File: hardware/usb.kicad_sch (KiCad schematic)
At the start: 4 parts

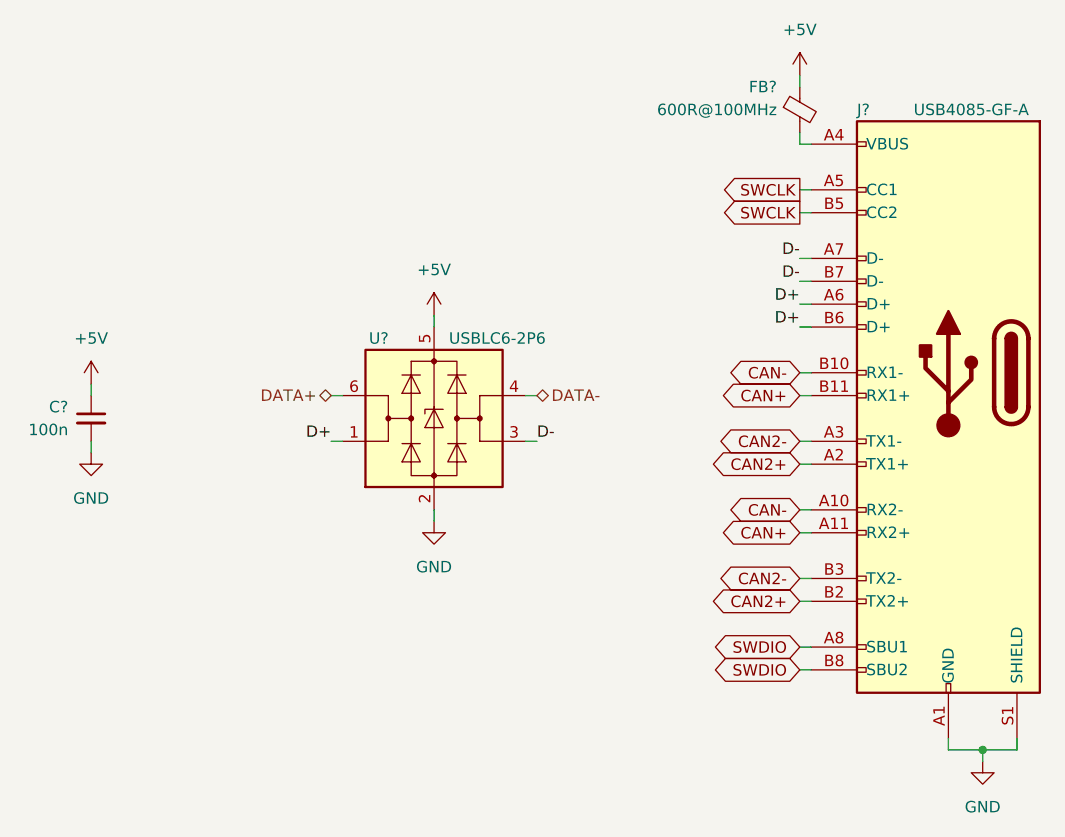
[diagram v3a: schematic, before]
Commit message: Improve the schematic according to the feedback
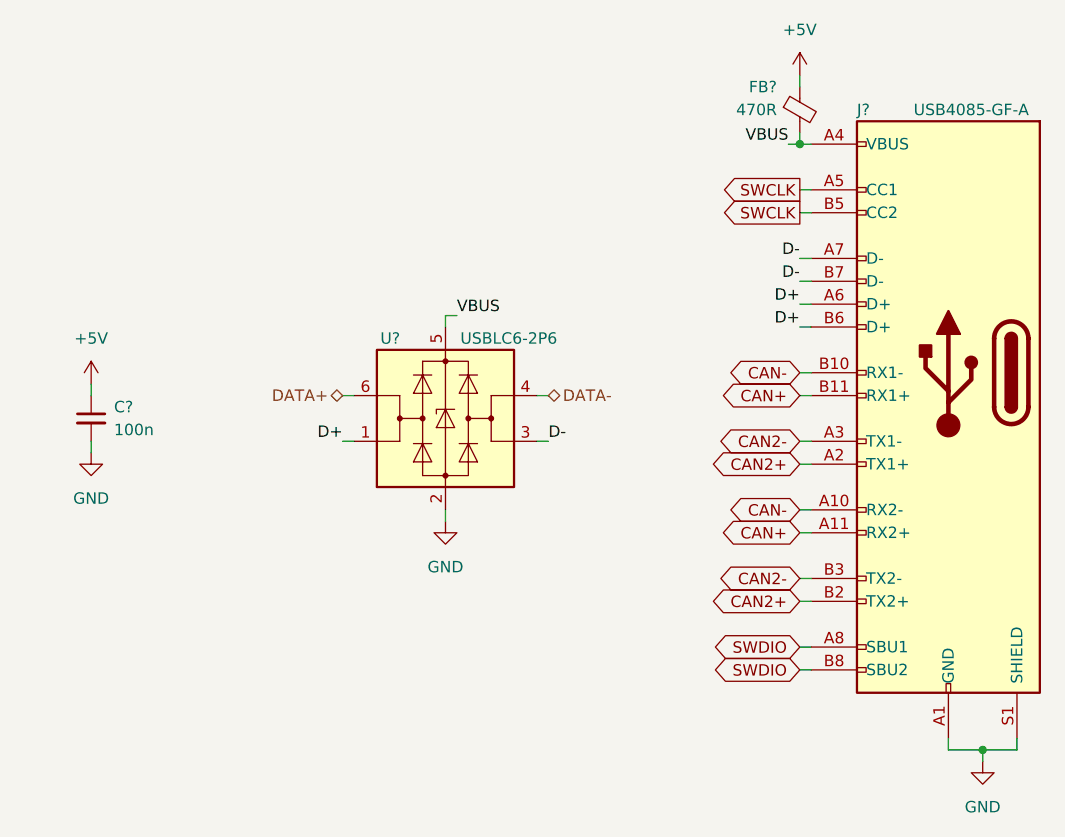
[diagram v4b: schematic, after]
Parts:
- FB?: value 600R@100MHz -> 470R
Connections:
- net +5V: no longer U?.5 (VBUS)
- net VBUS: now reaches FB?.2, J?.A4 (VBUS), J?.A9 (VBUS), J?.B4 (VBUS), J?.B9 (VBUS)
- net VBUS: now also U?.5 (VBUS)
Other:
- moved on the sheet: U?
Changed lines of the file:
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@@
   (junction (at 200.66 135.89) (diameter 0) (color 0 0 0 0)
   )
-  (wire (pts (xy 128.27 96.52) (xy 129.54 96.52))
+  (junction (at 180.34 68.58) (diameter 0) (color 0 0 0 0)
+  )
+  (wire (pts (xy 142.24 87.63) (xy 140.97 87.63))
+    (stroke (width 0) (type default))
+  )
+  (wire (pts (xy 129.54 96.52) (xy 130.81 96.52))
     (stroke (width 0) (type default))
   )
@@
     (stroke (width 0) (type default))
   )
-  (wire (pts (xy 139.7 87.63) (xy 139.7 88.9))
-    (stroke (width 0) (type default))
-  )
   (wire (pts (xy 180.34 83.82) (xy 181.61 83.82))
     (stroke (width 0) (type default))
   )
-  (wire (pts (xy 151.13 101.6) (xy 149.86 101.6))
+  (wire (pts (xy 152.4 101.6) (xy 151.13 101.6))
     (stroke (width 0) (type default))
   )
@@
     (stroke (width 0) (type default))
   )
-  (wire (pts (xy 128.27 101.6) (xy 129.54 101.6))
+  (wire (pts (xy 129.54 101.6) (xy 130.81 101.6))
     (stroke (width 0) (type default))
   )
@@
     (stroke (width 0) (type default))
   )
+  (wire (pts (xy 179.07 68.58) (xy 180.34 68.58))
+    (stroke (width 0) (type default))
+  )
   (wire (pts (xy 180.34 88.9) (xy 181.61 88.9))
     (stroke (width 0) (type default))
@@
     (stroke (width 0) (type default))
   )
+  (wire (pts (xy 140.97 87.63) (xy 140.97 88.9))
+    (stroke (width 0) (type default))
+  )
   (wire (pts (xy 101.6 95.25) (xy 101.6 96.52))
     (stroke (width 0) (type default))
@@
     (stroke (width 0) (type default))
   )
-  (wire (pts (xy 151.13 96.52) (xy 149.86 96.52))
-    (stroke (width 0) (type default))
-  )
-  (wire (pts (xy 139.7 109.22) (xy 139.7 110.49))
-    (stroke (width 0) (type default))
+  (wire (pts (xy 152.4 96.52) (xy 151.13 96.52))
+    (stroke (width 0) (type default))
+  )
+  (wire (pts (xy 140.97 109.22) (xy 140.97 110.49))
+    (stroke (width 0) (type default))
+  )
+  (label "VBUS" (at 179.07 68.58 180) (fields_autoplaced)
+    (effects (font (size 1.27 1.27)) (justify right bottom))
   )
   (label "D+" (at 180.34 86.36 180) (fields_autoplaced)
     (effects (font (size 1.27 1.27)) (justify right bottom))
   )
-  (label "D+" (at 128.27 101.6 180) (fields_autoplaced)
-    (effects (font (size 1.27 1.27)) (justify right bottom))
-  )
-  (label "D-" (at 151.13 101.6 0) (fields_autoplaced)
+  (label "D+" (at 129.54 101.6 180) (fields_autoplaced)
+    (effects (font (size 1.27 1.27)) (justify right bottom))
+  )
+  (label "D-" (at 152.4 101.6 0) (fields_autoplaced)
     (effects (font (size 1.27 1.27)) (justify left bottom))
   )
@@
     (effects (font (size 1.27 1.27)) (justify right bottom))
   )
+  (label "VBUS" (at 142.24 87.63 0) (fields_autoplaced)
+    (effects (font (size 1.27 1.27)) (justify left bottom))
+  )
   (label "D-" (at 180.34 83.82 180) (fields_autoplaced)
     (effects (font (size 1.27 1.27)) (justify right bottom))
@@
     )
   )
-  (hierarchical_label "DATA+" (shape bidirectional) (at 128.27 96.52 180) (fields_autoplaced)
-    (effects (font (size 1.27 1.27)) (justify right))
-  )
-  (hierarchical_label "DATA-" (shape bidirectional) (at 151.13 96.52 0) (fields_autoplaced)
+  (hierarchical_label "DATA+" (shape bidirectional) (at 129.54 96.52 180) (fields_autoplaced)
+    (effects (font (size 1.27 1.27)) (justify right))
+  )
+  (hierarchical_label "DATA-" (shape bidirectional) (at 152.4 96.52 0) (fields_autoplaced)
     (effects (font (size 1.27 1.27)) (justify left))
   )
@@
         )
         (path "/b652b05a-4e3d-4ad1-b032-18886abe7d45/1a71c66a-e6f2-4e7d-92f3-10826884049d"
-          (reference "#PWR0121") (unit 1)
+          (reference "#PWR050") (unit 1)
         )
       )
@@
         )
         (path "/b652b05a-4e3d-4ad1-b032-18886abe7d45/1a71c66a-e6f2-4e7d-92f3-10826884049d"
-          (reference "#PWR0124") (unit 1)
+          (reference "#PWR052") (unit 1)
         )
       )
@@
       (effects (font (size 1.27 1.27)) (justify right))
     )
-    (property "Value" "600R@100MHz" (at 177.8 64.77 0)
+    (property "Value" "470R" (at 177.8 64.77 0)
       (effects (font (size 1.27 1.27)) (justify right))
     )
@@
         )
         (path "/b652b05a-4e3d-4ad1-b032-18886abe7d45/1a71c66a-e6f2-4e7d-92f3-10826884049d"
-          (reference "FB7") (unit 1)
-        )
-      )
-    )
-  )
-  (symbol (lib_id "Power_Protection:USBLC6-2P6") (at 139.7 99.06 0) (unit 1)
-    (in_bom yes) (on_board yes) (dnp no)
-    (property "Reference" "U?" (at 132.4611 90.17 0)
+          (reference "FB2") (unit 1)
+        )
+      )
+    )
+  )
+  (symbol (lib_id "Power_Protection:USBLC6-2P6") (at 140.97 99.06 0) (unit 1)
+    (in_bom yes) (on_board yes) (dnp no)
+    (property "Reference" "U?" (at 133.7311 90.17 0)
       (effects (font (size 1.27 1.27)) (justify left))
     )
-    (property "Value" "USBLC6-2P6" (at 141.3511 90.17 0)
+    (property "Value" "USBLC6-2P6" (at 142.6211 90.17 0)
       (effects (font (size 1.27 1.27)) (justify left))
     )
-    (property "Footprint" "Package_TO_SOT_SMD:SOT-666" (at 139.7 111.76 0)
-      (effects (font (size 1.27 1.27)) hide)
-    )
-    (property "Datasheet" "https://www.st.com/resource/en/datasheet/usblc6-2.pdf" (at 144.78 90.17 0)
+    (property "Footprint" "Package_TO_SOT_SMD:SOT-666" (at 140.97 111.76 0)
+      (effects (font (size 1.27 1.27)) hide)
+    )
+    (property "Datasheet" "https://www.st.com/resource/en/datasheet/usblc6-2.pdf" (at 146.05 90.17 0)
       (effects (font (size 1.27 1.27)) hide)
     )
@@
         )
         (path "/b652b05a-4e3d-4ad1-b032-18886abe7d45/1a71c66a-e6f2-4e7d-92f3-10826884049d"
-          (reference "U13") (unit 1)
+          (reference "U5") (unit 1)
         )
       )
@@
         )
         (path "/b652b05a-4e3d-4ad1-b032-18886abe7d45/1a71c66a-e6f2-4e7d-92f3-10826884049d"
-          (reference "#PWR0120") (unit 1)
+          (reference "#PWR049") (unit 1)
         )
       )
@@
   (symbol (lib_id "power:GND") (at 200.66 137.16 0) (unit 1)
     (in_bom yes) (on_board yes) (dnp no) (fields_autoplaced)
-    (property "Reference" "#PWR0125" (at 200.66 143.51 0)
+    (property "Reference" "#PWR053" (at 200.66 143.51 0)
       (effects (font (size 1.27 1.27)) hide)
     )
@@
       (project "rearbox"
         (path "/b652b05a-4e3d-4ad1-b032-18886abe7d45/1a71c66a-e6f2-4e7d-92f3-10826884049d"
-          (reference "#PWR0125") (unit 1)
-        )
-      )
-    )
-  )
-  (symbol (lib_id "power:GND") (at 139.7 110.49 0) (unit 1)
-    (in_bom yes) (on_board yes) (dnp no)
-    (property "Reference" "#PWR?" (at 139.7 116.84 0)
-      (effects (font (size 1.27 1.27)) hide)
-    )
-    (property "Value" "GND" (at 139.7 115.57 0)
-      (effects (font (size 1.27 1.27)))
-    )
-    (property "Footprint" "" (at 139.7 110.49 0)
-      (effects (font (size 1.27 1.27)) hide)
-    )
-    (property "Datasheet" "" (at 139.7 110.49 0)
+          (reference "#PWR053") (unit 1)
+        )
+      )
+    )
+  )
+  (symbol (lib_id "power:GND") (at 140.97 110.49 0) (unit 1)
+    (in_bom yes) (on_board yes) (dnp no)
+    (property "Reference" "#PWR?" (at 140.97 116.84 0)
+      (effects (font (size 1.27 1.27)) hide)
+    )
+    (property "Value" "GND" (at 140.97 115.57 0)
+      (effects (font (size 1.27 1.27)))
+    )
+    (property "Footprint" "" (at 140.97 110.49 0)
+      (effects (font (size 1.27 1.27)) hide)
+    )
+    (property "Datasheet" "" (at 140.97 110.49 0)
       (effects (font (size 1.27 1.27)) hide)
     )
@@
         )
         (path "/b652b05a-4e3d-4ad1-b032-18886abe7d45/1a71c66a-e6f2-4e7d-92f3-10826884049d"
-          (reference "#PWR0123") (unit 1)
+          (reference "#PWR051") (unit 1)
         )
       )
@@
     )
   )
-  (symbol (lib_id "power:+5V") (at 139.7 87.63 0) (unit 1)
-    (in_bom yes) (on_board yes) (dnp no)
-    (property "Reference" "#PWR?" (at 139.7 91.44 0)
-      (effects (font (size 1.27 1.27)) hide)
-    )
-    (property "Value" "+5V" (at 139.7 82.55 0)
-      (effects (font (size 1.27 1.27)))
-    )
-    (property "Footprint" "" (at 139.7 87.63 0)
-      (effects (font (size 1.27 1.27)) hide)
-    )
-    (property "Datasheet" "" (at 139.7 87.63 0)
-      (effects (font (size 1.27 1.27)) hide)
-    )
-    (pin "1")
-    (instances
-      (project "rearbox"
-        (path "/b652b05a-4e3d-4ad1-b032-18886abe7d45"
-          (reference "#PWR?") (unit 1)
-        )
-        (path "/b652b05a-4e3d-4ad1-b032-18886abe7d45/1a71c66a-e6f2-4e7d-92f3-10826884049d"
-          (reference "#PWR0122") (unit 1)
-        )
-      )
-    )
-  )
-  (symbol (lib_id "Device:C_Small") (at 101.6 99.06 0) (mirror y) (unit 1)
-    (in_bom yes) (on_board yes) (dnp no)
-    (property "Reference" "C?" (at 99.06 97.79 0)
+  (symbol (lib_id "Device:C_Small") (at 101.6 99.06 0) (unit 1)
+    (in_bom yes) (on_board yes) (dnp no)
+    (property "Reference" "C?" (at 104.14 97.79 0)
       (effects (font (size 1.27 1.27)) (justify left))
     )
-    (property "Value" "100n" (at 99.06 100.33 0)
+    (property "Value" "100n" (at 104.14 100.33 0)
       (effects (font (size 1.27 1.27)) (justify left))
     )
@@
         )
         (path "/b652b05a-4e3d-4ad1-b032-18886abe7d45/1a71c66a-e6f2-4e7d-92f3-10826884049d"
-          (reference "C36") (unit 1)
-        )
-      )
+          (reference "C25") (unit 1)
+        )
+      )
